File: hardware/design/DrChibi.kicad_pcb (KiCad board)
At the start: 4 copper layers, 143.5 x 14 mm, 274 parts, among them P1 CONN_02X05, P2 PAD_SMD, P3 IN+, P4 IN-, P5 CONN_01X04, U1 STM32F40X_LQFP64, U2 ISO1050, X1 MINI-USB-SHIELD-32005-201, X2 8MHz 10ppm

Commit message: Updated B.SilkS
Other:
- board text added: "Stronger"
- board text removed: "stronger"
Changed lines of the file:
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@@
-(kicad_pcb (version 4) (host pcbnew 4.1.0-alpha+201608050946+7006~46~ubuntu16.04.1-product)
+(kicad_pcb (version 20160815) (host pcbnew 4.1.0-alpha+201608161231+7059~46~ubuntu16.04.1-product)
   (general
     (links 657)
     (no_connects 0)
-    (area 34.424999 92.939999 178.075001 107.060001)
+    (area 17.887762 85.370143 194.736238 113.328971)
     (thickness 1.6)
     (drawings 43)
@@
   (page A4)
   (title_block
-    (title DrChibi)
-    (date 2016-01-31)
-    (rev 0)
+    (title "DrChibi, Looong-Strip")
+    (date 2016-08-17)
+    (rev 1.0)
+    (company "Jörg Wangemann")
+    (comment 1 "6-Phase Motor Controller / Inverter")
+    (comment 4 "CC-BY-SA 4.0")
   )
   (layers
@@
     (uvia_dia 0.6)
     (uvia_drill 0.3)
+    (diff_pair_gap 0.25)
+    (diff_pair_width 0.2)
     (add_net "/CAN bus transceiver/CANH")
     (add_net "/CAN bus transceiver/CANL")
@@
     (uvia_dia 0.6)
     (uvia_drill 0.3)
+    (diff_pair_gap 0.25)
+    (diff_pair_width 0.2)
     (add_net +5V)
   )
@@
     (uvia_dia 0.6)
     (uvia_drill 0.3)
+    (diff_pair_gap 0.25)
+    (diff_pair_width 0.2)
     (add_net +24V)
   )
@@
     (uvia_dia 0.6)
     (uvia_drill 0.3)
+    (diff_pair_gap 0.25)
+    (diff_pair_width 0.2)
     (add_net +3V3)
   )
@@
     (effects (font (size 1 1) (thickness 0.25)) (justify mirror))
   )
-  (gr_text stronger (at 137.808 105.334) (layer B.SilkS)
+  (gr_text Stronger (at 137.7064 103.937) (layer B.SilkS)
     (effects (font (size 0.9 0.9) (thickness 0.2)) (justify mirror))
   )
-  (gr_text Stepper (at 137.808 103.937) (layer B.SilkS)
+  (gr_text Stepper (at 137.7826 105.3848) (layer B.SilkS)
     (effects (font (size 0.9 1) (thickness 0.2)) (justify mirror))
   )

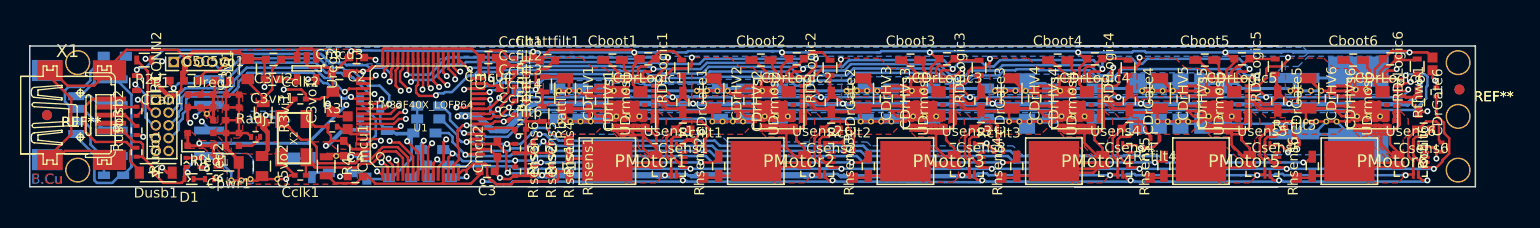
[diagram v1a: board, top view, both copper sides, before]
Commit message: Added "just-in-case-" pads at PWM d,e,f.
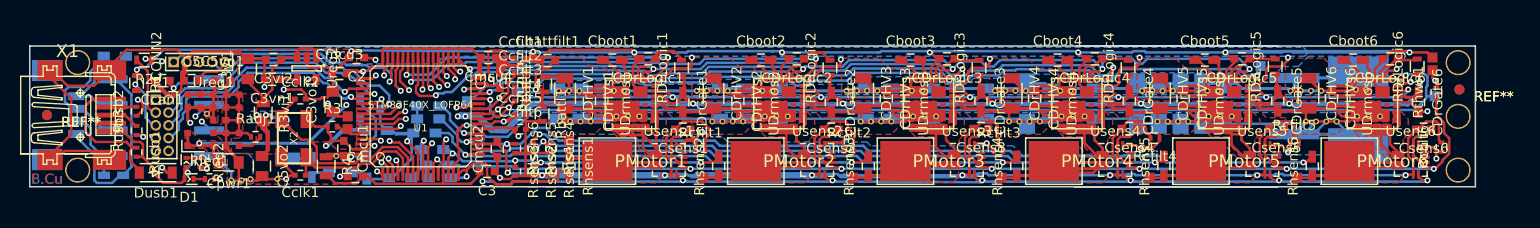
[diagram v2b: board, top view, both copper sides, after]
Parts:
- added P_PWM1: PAD_SMD, Pads:PAD_SMD_1x1, B.Cu at (77.9, 98.5)
- added P_PWM2: PAD_SMD, Pads:PAD_SMD_1x1, B.Cu at (156.7, 95.0)
- added P_PWM3: PAD_SMD, Pads:PAD_SMD_1x1, B.Cu at (174.0, 98.0)
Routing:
- net /Half Bridge D/PWM: track 72.6 -> 74.8 mm
- net /Half Bridge E/PWM: track 83.5 -> 84.6 mm
- net /Half Bridge F/PWM: track 109.4 -> 110.3 mm
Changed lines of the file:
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@@
-(kicad_pcb (version 20160815) (host pcbnew 4.1.0-alpha+201608161231+7059~46~ubuntu16.04.1-product)
+(kicad_pcb (version 20160815) (host pcbnew 4.1.0-alpha+201609031632+7111~49~ubuntu16.04.1-product)
   (general
-    (links 657)
+    (links 660)
     (no_connects 0)
-    (area 17.887762 85.370143 194.736238 113.328971)
+    (area 34.424999 92.939999 178.075001 107.060001)
     (thickness 1.6)
     (drawings 43)
-    (tracks 3765)
+    (tracks 3775)
     (zones 0)
-    (modules 274)
+    (modules 277)
     (nets 106)
   )
@@
       (net 4 +3V3))
   )
+  (module Pads:PAD_SMD_1x1 (layer B.Cu)
+    (at 77.9148 98.5014)
+    (fp_text reference P_PWM1 (at 0 -2.5) (layer B.Fab)
+      (effects (font (size 1 1) (thickness 0.15)) (justify mirror))
+    )
+    (fp_text value PAD_SMD (at 0 2.2) (layer B.Fab)
+      (effects (font (size 1 1) (thickness 0.15)) (justify mirror))
+    )
+    (pad 1 smd rect (at 0 0) (size 1 1) (layers B.Cu B.Mask)
+      (net 58 "/Half Bridge D/PWM"))
+  )
+  (module Pads:PAD_SMD_1x1 (layer B.Cu)
+    (at 156.6802 94.9962)
+    (fp_text reference P_PWM2 (at 0 -2.5) (layer B.Fab)
+      (effects (font (size 1 1) (thickness 0.15)) (justify mirror))
+    )
+    (fp_text value PAD_SMD (at 0 2.2) (layer B.Fab)
+      (effects (font (size 1 1) (thickness 0.15)) (justify mirror))
+    )
+    (pad 1 smd rect (at 0 0) (size 1 1) (layers B.Cu B.Mask)
+      (net 82 "/Half Bridge E/PWM"))
+  )
+  (module Pads:PAD_SMD_1x1 (layer B.Cu)
+    (at 173.9522 97.9934)
+    (fp_text reference P_PWM3 (at 0 -2.5) (layer B.Fab)
+      (effects (font (size 1 1) (thickness 0.15)) (justify mirror))
+    )
+    (fp_text value PAD_SMD (at 0 2.2) (layer B.Fab)
+      (effects (font (size 1 1) (thickness 0.15)) (justify mirror))
+    )
+    (pad 1 smd rect (at 0 0) (size 1 1) (layers B.Cu B.Mask)
+      (net 81 "/Half Bridge F/PWM"))
+  )
   (gr_text "F R E E\nhardware design" (at 73.4444 95.5804) (layer B.SilkS)
     (effects (font (size 1 1) (thickness 0.25)) (justify mirror))
@@
   (via (at 69.4185 98.2855) (size 0.6) (drill 0.3) (layers F.Cu B.Cu) (net 57))
   (segment (start 68.95368 98.75032) (end 69.4185 98.2855) (width 0.25) (layer F.Cu) (net 57))
+  (segment (start 79.4515 97.2695) (end 79.5658 97.1552) (width 0.25) (layer B.Cu) (net 58))
+  (segment (start 79.5658 97.1552) (end 79.734344 96.986656) (width 0.25) (layer B.Cu) (net 58))
+  (segment (start 78.4736 98.095) (end 78.626 98.095) (width 0.25) (layer B.Cu) (net 58))
+  (segment (start 78.626 98.095) (end 79.5658 97.1552) (width 0.25) (layer B.Cu) (net 58))
+  (segment (start 78.0672 98.5014) (end 78.4736 98.095) (width 0.25) (layer B.Cu) (net 58))
+  (segment (start 77.9148 98.5014) (end 78.0672 98.5014) (width 0.25) (layer B.Cu) (net 58))
   (segment (start 77.61 97.333) (end 77.6735 97.2695) (width 0.25) (layer B.Cu) (net 58))
   (segment (start 95.771 96.444) (end 97.085498 96.444) (width 0.25) (layer B.Cu) (net 58))
   (segment (start 77.6735 97.2695) (end 79.4515 97.2695) (width 0.25) (layer B.Cu) (net 58))
   (segment (start 92.716522 95.802522) (end 92.85 95.936) (width 0.25) (layer B.Cu) (net 58))
-  (segment (start 79.4515 97.2695) (end 79.734344 96.986656) (width 0.25) (layer B.Cu) (net 58))
   (segment (start 79.734344 96.986656) (end 80.559844 96.986656) (width 0.25) (layer B.Cu) (net 58))
   (segment (start 95.263 95.936) (end 95.771 96.444) (width 0.25) (layer B.Cu) (net 58))
@@
   (segment (start 171.844 96.19) (end 171.844 95.428) (width 0.25) (layer In2.Cu) (net 80))
   (segment (start 171.59 96.444) (end 171.844 96.19) (width 0.25) (layer In2.Cu) (net 80))
+  (segment (start 173.114 98.222) (end 173.114 97.9426) (width 0.25) (layer B.Cu) (net 81))
+  (segment (start 173.9522 97.9934) (end 173.1648 97.9934) (width 0.25) (layer B.Cu) (net 81))
+  (segment (start 173.114 97.9426) (end 173.114 97.079) (width 0.25) (layer B.Cu) (net 81))
+  (segment (start 173.1648 97.9934) (end 173.114 97.9426) (width 0.25) (layer B.Cu) (net 81))
   (segment (start 76.975 101.397) (end 77.483 100.889) (width 0.25) (layer F.Cu) (net 81))
   (segment (start 77.483 100.889) (end 77.864 100.889) (width 0.25) (layer F.Cu) (net 81))
@@
   (segment (start 173.241 96.952) (end 173.241 96.063) (width 0.25) (layer B.Cu) (net 81))
   (segment (start 173.114 97.079) (end 173.241 96.952) (width 0.25) (layer B.Cu) (net 81))
-  (segment (start 173.114 98.222) (end 173.114 97.079) (width 0.25) (layer B.Cu) (net 81))
   (segment (start 85.611 99.365) (end 85.103 99.365) (width 0.25) (layer B.Cu) (net 81))
   (segment (start 79.769 102.032) (end 81.928 102.032) (width 0.25) (layer B.Cu) (net 81))
@@
   (segment (start 84.595 99.365) (end 85.103 99.365) (width 0.25) (layer B.Cu) (net 81))
   (segment (start 85.611 99.365) (end 85.484 99.365) (width 0.25) (layer B.Cu) (net 81))
+  (segment (start 156.35 95.936) (end 156.35 95.3264) (width 0.25) (layer B.Cu) (net 82))
+  (segment (start 156.35 95.3264) (end 156.6802 94.9962) (width 0.25) (layer B.Cu) (net 82))
   (segment (start 85.1665 96.6345) (end 85.179024 96.6345) (width 0.25) (layer B.Cu) (net 82))
   (segment (start 85.179024 96.6345) (end 85.572724 96.2408) (width 0.25) (layer B.Cu) (net 82))

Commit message: Swapped STM32 Pin33 and Pin50 and added some pads to enable usage of USART3 when TIM8 is bridged to PWM d,e,f.
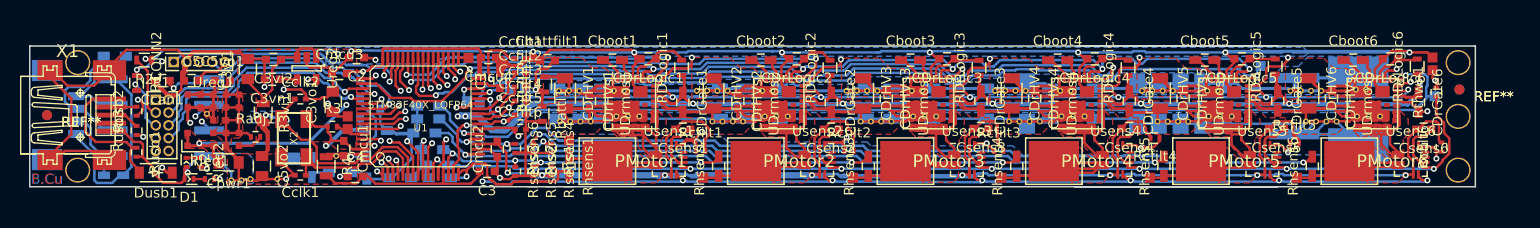
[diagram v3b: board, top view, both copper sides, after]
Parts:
- added P_PWM4: PAD_SMD, Pads:PAD_SMD_1x1, B.Cu at (79.2, 98.8)
- added P_PWM5: PAD_SMD, Pads:PAD_SMD_1x1, B.Cu at (82.2, 97.4)
- added P_USART3_CLK1: PAD_SMD, Pads:PAD_SMD_1x1, F.Cu at (78.0, 94.2)
- moved P2 0.91 mm to (83.7, 97.2)
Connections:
- U1 pad 33: /Half Bridge A/ZCD_EN -> /MCU/LED3
- U1 pad 50: (no net) -> /Half Bridge A/ZCD_EN
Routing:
- net /Half Bridge A/ZCD_EN: track 110.8 -> 122.1 mm
- net /MCU/LED3: track 0.00 -> 1.09 mm
- net /Half Bridge D/PWM: track 74.8 -> 75.7 mm
- net /Half Bridge E/PWM: track 84.6 -> 85.3 mm
- net /MCU/AN_IN: track 30.7 -> 30.0 mm

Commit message: Changed statement in B.Silk.
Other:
- board text added: "Autopilot"
- board text added: "Made on planet Earth, drive for peace"
- board text removed: "CC-BY-SA"
- board text removed: "flight for peace"

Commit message: Prepare for fab.
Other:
- board text added: "Self Sensing Motor Controller"
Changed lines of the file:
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@@
-(kicad_pcb (version 20160815) (host pcbnew 4.1.0-alpha+201609130817+7147~55~ubuntu16.04.1-)
+(kicad_pcb (version 20160815) (host pcbnew no-vcs-found-undefined)
   (general
     (links 663)
     (no_connects 0)
-    (area 34.424999 92.939999 178.075001 107.060001)
+    (area 17.887762 85.370143 194.736238 113.328971)
     (thickness 1.6)
-    (drawings 43)
+    (drawings 44)
     (tracks 3784)
     (zones 0)
@@
     (visible_elements FFFCFF7F)
     (pcbplotparams
-      (layerselection 0x00030_ffffffff)
+      (layerselection 0x010dc_ffffffff)
       (usegerberextensions true)
       (excludeedgelayer true)
@@
       (net 106 /MCU/LED3))
   )
+  (gr_text "Self Sensing Motor Controller" (at 147.3076 94.4374) (layer B.SilkS)
+    (effects (font (size 1.4 1.35) (thickness 0.25)) (justify mirror))
+  )
   (gr_text "Made on planet Earth, drive for peace" (at 105.8548 102.1844) (layer B.SilkS)
     (effects (font (size 1 1.08) (thickness 0.2)) (justify mirror))
@@
     (effects (font (size 1 1) (thickness 0.25)) (justify mirror))
   )
-  (gr_text Stronger (at 137.7064 103.937) (layer B.SilkS)
+  (gr_text Stronger (at 144.8946 103.8862) (layer B.SilkS)
     (effects (font (size 0.9 0.9) (thickness 0.2)) (justify mirror))
   )
-  (gr_text Stepper (at 137.7826 105.3848) (layer B.SilkS)
+  (gr_text Stepper (at 144.9708 105.334) (layer B.SilkS)
     (effects (font (size 0.9 1) (thickness 0.2)) (justify mirror))
   )
-  (gr_text "no cry" (at 145.1486 105.2832) (layer B.SilkS)
-    (effects (font (size 0.9 0.9) (thickness 0.2)) (justify mirror))
+  (gr_text "no cry" (at 127.2924 95.5042) (layer B.SilkS)
+    (effects (font (size 1 1) (thickness 0.2)) (justify mirror))
   )
   (gr_text BLDC (at 151.2954 105.334) (layer B.SilkS)
@@
     (effects (font (size 2.4 1.2) (thickness 0.25)) (justify mirror))
   )
-  (gr_text "no sensors" (at 144.9962 103.9116) (layer B.SilkS)
-    (effects (font (size 0.9 0.8) (thickness 0.2)) (justify mirror))
+  (gr_text "no sensors" (at 127.2924 94.0056) (layer B.SilkS)
+    (effects (font (size 1 0.9) (thickness 0.2)) (justify mirror))
   )
-  (gr_text P (at 133.0836 104.064) (layer B.SilkS)
+  (gr_text P (at 139.1796 103.81) (layer B.SilkS)
     (effects (font (size 1 1.2) (thickness 0.25)) (justify mirror))
   )
-  (gr_text Autopilot (at 129.8324 105.4102) (layer B.SilkS)
-    (effects (font (size 0.8 0.8) (thickness 0.2)) (justify mirror))
+  (gr_text Autopilot (at 136.1316 105.3594) (layer B.SilkS)
+    (effects (font (size 0.9 1) (thickness 0.2)) (justify mirror))
   )
-  (gr_text APARAZZI (at 129.2736 104.191) (layer B.SilkS)
+  (gr_text APARAZZI (at 135.522 103.937) (layer B.SilkS)
     (effects (font (size 0.8 0.9) (thickness 0.2)) (justify mirror))
   )

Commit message: Little change on B.Silks
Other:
- board text added: "Self Sensing Motor Drive"
- board text removed: "Self Sensing Motor Controller"
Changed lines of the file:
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@@
     (links 663)
     (no_connects 0)
-    (area 17.887762 85.370143 194.736238 113.328971)
+    (area 34.424999 92.939999 178.075001 107.060001)
     (thickness 1.6)
     (drawings 44)
@@
   )
   (layers
-    (0 F.Cu signal)
-    (1 In1.Cu mixed)
-    (2 In2.Cu mixed)
-    (31 B.Cu signal)
-    (33 F.Adhes user)
-    (34 B.Paste user)
-    (35 F.Paste user)
+    (0 F.Cu signal hide)
+    (1 In1.Cu mixed hide)
+    (2 In2.Cu mixed hide)
+    (31 B.Cu signal hide)
+    (33 F.Adhes user hide)
+    (34 B.Paste user hide)
+    (35 F.Paste user hide)
     (36 B.SilkS user)
-    (37 F.SilkS user)
-    (38 B.Mask user)
-    (39 F.Mask user)
-    (40 Dwgs.User user)
+    (37 F.SilkS user hide)
+    (38 B.Mask user hide)
+    (39 F.Mask user hide)
+    (40 Dwgs.User user hide)
     (41 Cmts.User user)
     (42 Eco1.User user)
@@
       (net 106 /MCU/LED3))
   )
-  (gr_text "Self Sensing Motor Controller" (at 147.3076 94.4374) (layer B.SilkS)
-    (effects (font (size 1.4 1.35) (thickness 0.25)) (justify mirror))
+  (gr_text "Self Sensing Motor Drive" (at 148.2728 94.3866) (layer B.SilkS)
+    (effects (font (size 1.5 1.5) (thickness 0.25)) (justify mirror))
   )
-  (gr_text "Made on planet Earth, drive for peace" (at 105.8548 102.1844) (layer B.SilkS)
-    (effects (font (size 1 1.08) (thickness 0.2)) (justify mirror))
+  (gr_text "Made on planet Earth, drive for peace" (at 105.7786 102.159) (layer B.SilkS)
+    (effects (font (size 1.3 1.23) (thickness 0.2)) (justify mirror))
   )
   (gr_text "F R E E\nhardware design" (at 73.4444 95.5804) (layer B.SilkS)
-    (effects (font (size 1 1) (thickness 0.25)) (justify mirror))
+    (effects (font (size 1.2 1.2) (thickness 0.25)) (justify mirror))
   )
-  (gr_text Stronger (at 144.8946 103.8862) (layer B.SilkS)
+  (gr_text Stronger (at 143.4214 103.8862) (layer B.SilkS)
     (effects (font (size 0.9 0.9) (thickness 0.2)) (justify mirror))
   )
-  (gr_text Stepper (at 144.9708 105.334) (layer B.SilkS)
+  (gr_text Stepper (at 143.4722 105.334) (layer B.SilkS)
     (effects (font (size 0.9 1) (thickness 0.2)) (justify mirror))
   )
-  (gr_text "no cry" (at 127.2924 95.5042) (layer B.SilkS)
-    (effects (font (size 1 1) (thickness 0.2)) (justify mirror))
+  (gr_text "no cry" (at 129.299 95.4026) (layer B.SilkS)
+    (effects (font (size 1.2 1.2) (thickness 0.2)) (justify mirror))
   )
-  (gr_text BLDC (at 151.2954 105.334) (layer B.SilkS)
+  (gr_text BLDC (at 150.3556 105.334) (layer B.SilkS)
     (effects (font (size 0.9 0.9) (thickness 0.2)) (justify mirror))
   )
-  (gr_text PMSM (at 151.27 103.9624) (layer B.SilkS)
+  (gr_text PMSM (at 150.3556 103.937) (layer B.SilkS)
     (effects (font (size 0.9 0.8) (thickness 0.2)) (justify mirror))
   )
-  (gr_text "Power for" (at 158.3058 104.572) (layer B.SilkS)
+  (gr_text "Power for" (at 157.5946 104.572) (layer B.SilkS)
     (effects (font (size 2.4 1.2) (thickness 0.25)) (justify mirror))
   )
-  (gr_text "no sensors" (at 127.2924 94.0056) (layer B.SilkS)
-    (effects (font (size 1 0.9) (thickness 0.2)) (justify mirror))
+  (gr_text "no sensors" (at 129.3752 93.9294) (layer B.SilkS)
+    (effects (font (size 1.2 1) (thickness 0.2)) (justify mirror))
   )
-  (gr_text P (at 139.1796 103.81) (layer B.SilkS)
+  (gr_text P (at 137.9858 103.7846) (layer B.SilkS)
     (effects (font (size 1 1.2) (thickness 0.25)) (justify mirror))
   )
-  (gr_text Autopilot (at 136.1316 105.3594) (layer B.SilkS)
+  (gr_text Autopilot (at 134.9378 105.3594) (layer B.SilkS)
     (effects (font (size 0.9 1) (thickness 0.2)) (justify mirror))
   )
-  (gr_text APARAZZI (at 135.522 103.937) (layer B.SilkS)
+  (gr_text APARAZZI (at 134.3536 103.937) (layer B.SilkS)
     (effects (font (size 0.8 0.9) (thickness 0.2)) (justify mirror))
   )
@@
   )
   (gr_text "DrChibi, Looong-Strip" (at 105.7024 94.8946) (layer B.SilkS)
-    (effects (font (size 2 2) (thickness 0.3)) (justify mirror))
+    (effects (font (size 2 2.19) (thickness 0.3)) (justify mirror))
   )
   (gr_text github.com/joewa/ChibiESC (at 105.8548 104.6482) (layer B.SilkS)
-    (effects (font (size 1.5 1.5) (thickness 0.25)) (justify mirror))
+    (effects (font (size 1.6 1.7) (thickness 0.25)) (justify mirror))
   )
   (gr_text B.Cu (at 36.208 106.223) (layer B.Cu)
